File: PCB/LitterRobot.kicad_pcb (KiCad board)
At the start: 4 copper layers, 55 x 140 mm, 155 parts, among them J1 DF11C-4DP-2V(57), J2 DF11C-6DP-2V(57), J3 DF11C-8DP-2V(57), J4 DF11C-6DP-2V(57), J5 TSM-105-01-S-DV, Q1 BSS138, Q10 BC817, Q11 BC817, Q12 BC817, Q13 BC817, Q14 BC817, Q15 BC817, Q16 BC817, Q17 BC817, Q18 BC817, Q19 BC817, Q2 BSS138, Q20 BC817, Q21 BC817, Q22 BC817, Q23 BC817, Q24 BC817, Q3 BC817, Q4 BC817, Q5 BC817, Q6 BC817, Q7 BC817, Q8 BC817, Q9 BC817, SW1 PCB_Push_Button, SW2 PCB_Push_Button, SW3 PCB_Push_Button, SW4 PCB_Push_Button, SW5 PCB_Push_Button, SW6 PCB_Push_Button, U1 MPM54304GMN-0001, U2 10CL016YE144C8G, U3 S25FL128SAGMFI000, U4 EMB1061, U5 DRV8871DDA, U6 MCP1700T-5002E/TT, U7 VEML6035, X1 X1G0044510011

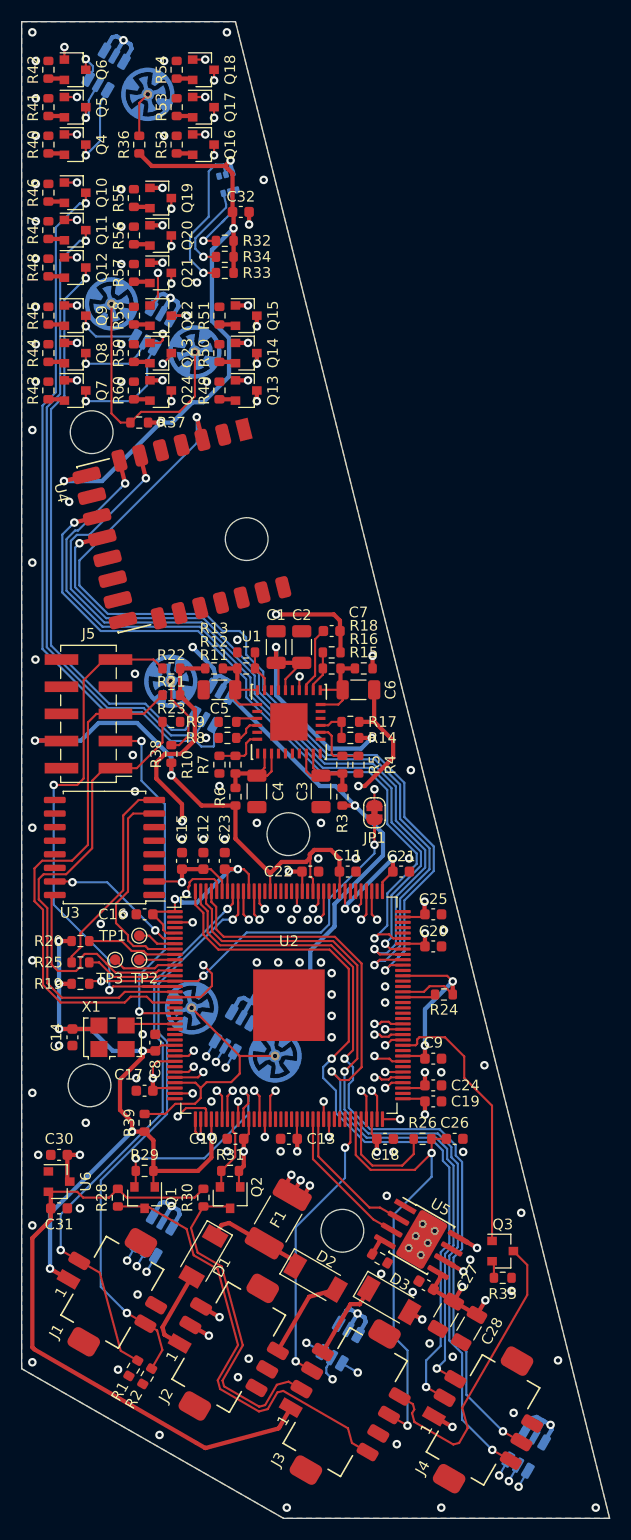
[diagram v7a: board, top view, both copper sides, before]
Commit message: Increase via drill size to 0.45 mm
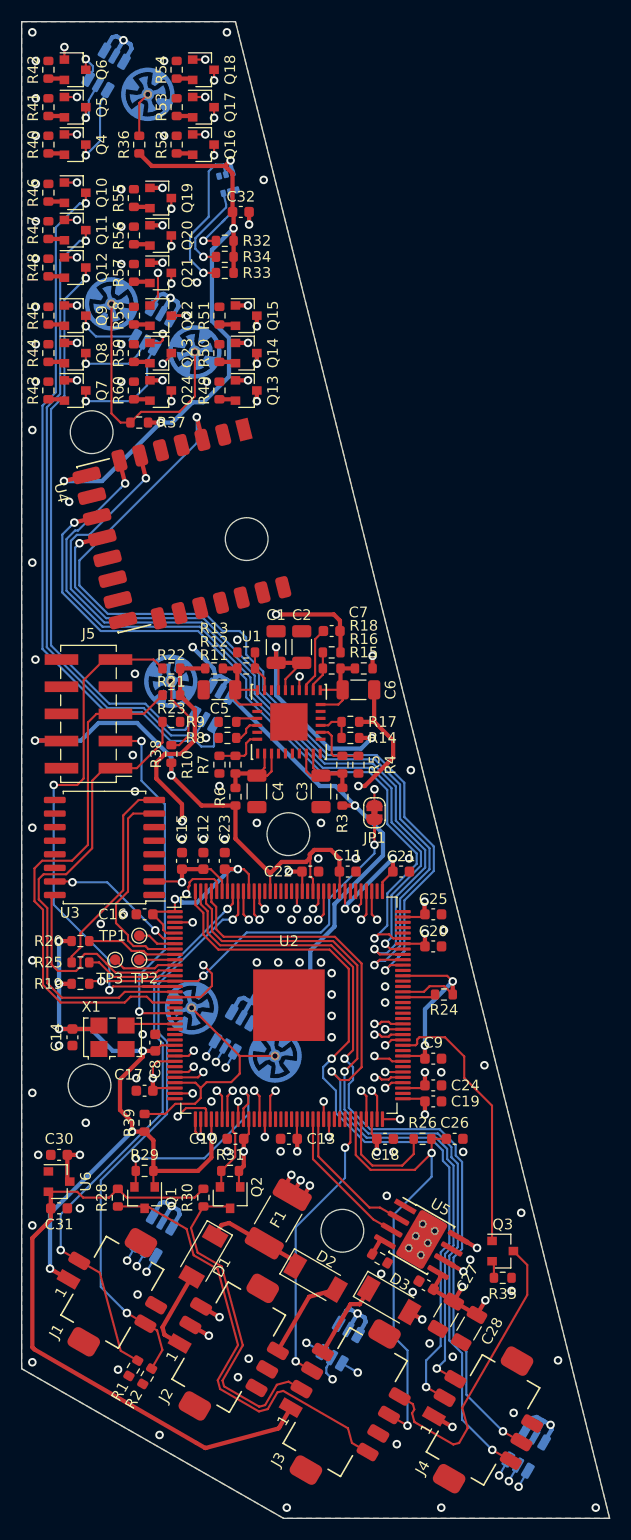
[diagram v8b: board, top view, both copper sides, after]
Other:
- net class Default: via_drill 0.4 -> 0.45
- rule via_min_size: 0.4 -> 0.8
